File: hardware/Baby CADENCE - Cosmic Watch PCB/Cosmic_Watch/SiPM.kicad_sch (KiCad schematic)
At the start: 1 part, among them IC1 MICROFJ-60035-TSV-TR1

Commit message: Comments/Reminders
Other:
- note added: "Implement Bias Decoupling"
- note added: "Implement Bias Filter (here or in the signal processing schematic)"
- note added: "Implement Impedence Matching"
- moved on the sheet: IC1

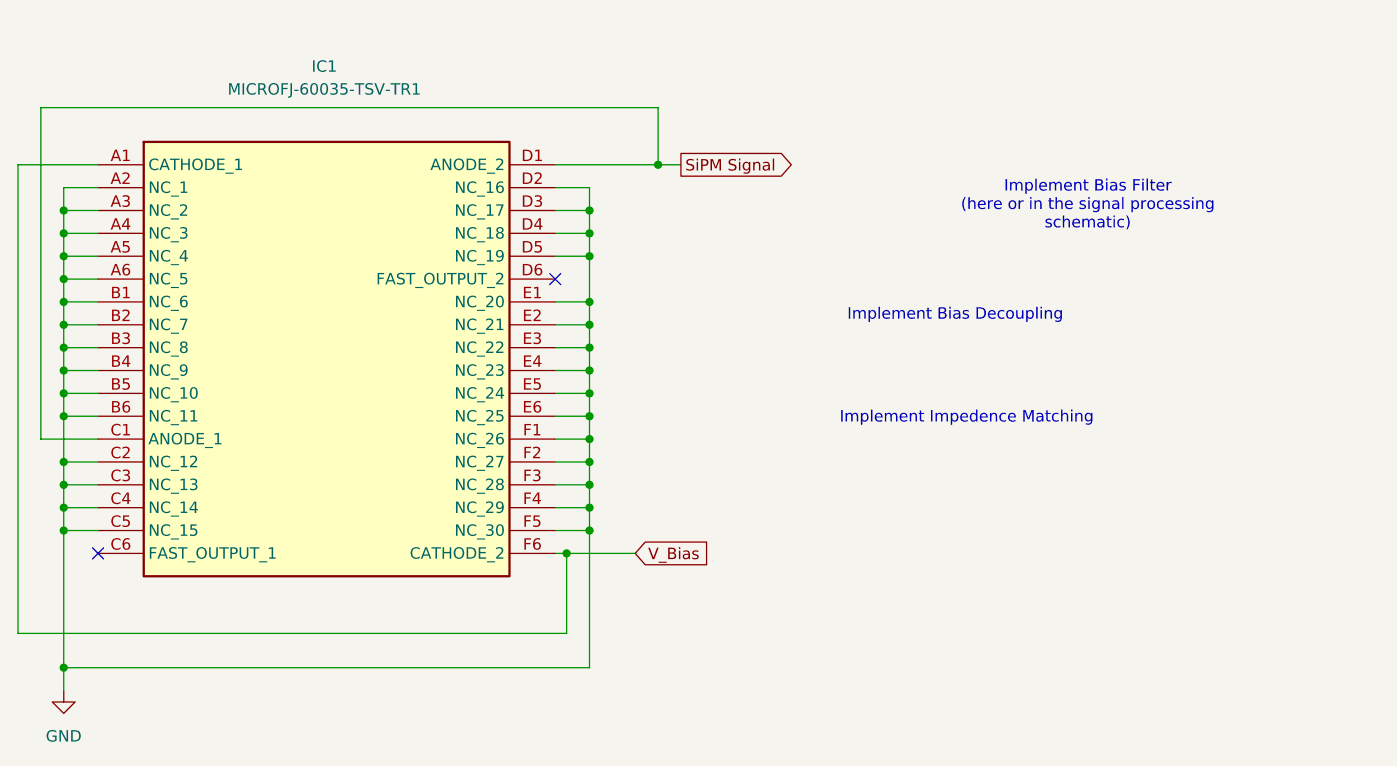
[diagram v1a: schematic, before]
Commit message: More Updates
Almost done with power.sch, just need to figure out ferrite bead values/other manufacturers since the old one is obsolete. Still figuring out values for the amplification stage.
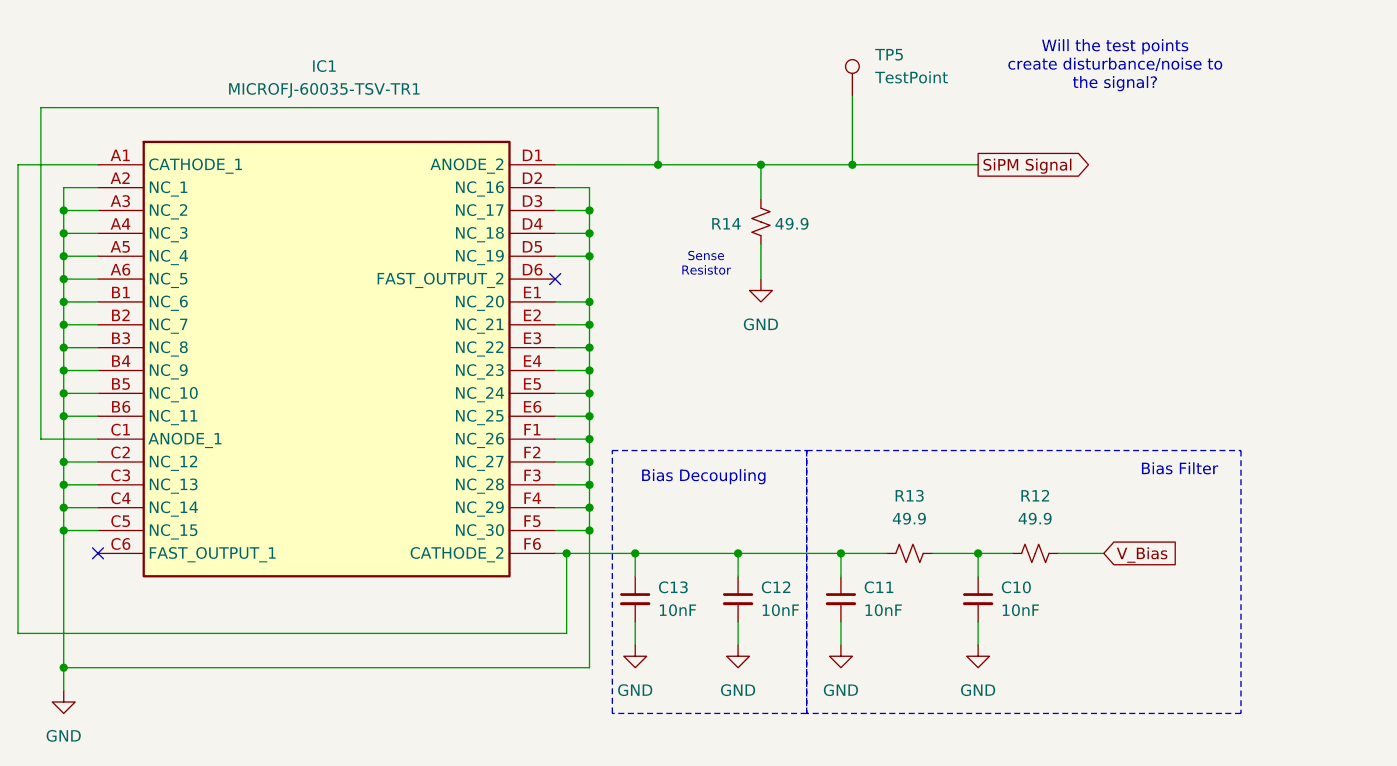
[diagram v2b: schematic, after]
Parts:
- added C10, C11, C12, C13: 10nF, symbol Device:C_Small
- added R12, R13, R14: 49.9, symbol Device:R_Small_US
- added TP5: TestPoint, symbol Connector:TestPoint
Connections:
- net GND: now also C10.2, C11.2, C12.2, C13.2, R14.2
- net SiPM Signal: now also R14.1, TP5.1
- net V_Bias: now also R12.2; no longer IC1.A1 (CATHODE_1), IC1.F6 (CATHODE_2)
- new net: C11.1, C12.1, C13.1, IC1.A1 (CATHODE_1), IC1.F6 (CATHODE_2), R13.1
- new net: C10.1, R12.1, R13.2
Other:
- note added: "Bias Decoupling"
- note added: "Bias Filter"
- note added: "Sense Resistor"
- note added: "Will the test points create disturbance/noise to the signal?"
- note removed: "Implement Bias Decoupling"
- note removed: "Implement Bias Filter (here or in the signal processing schematic)"
- note removed: "Implement Impedence Matching"

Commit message: Updates
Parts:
- TP5: value TestPoint -> Raw Signal Test Point
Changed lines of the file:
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@@
 	(text "Will the test points \ncreate disturbance/noise to\nthe signal?\n"
 		(exclude_from_sim no)
-		(at 154.94 24.638 0)
+		(at 167.894 22.86 0)
 		(effects
 			(font
@@
 		(on_board yes)
 		(dnp no)
-		(fields_autoplaced yes)
 		(property "Reference" "TP5"
-			(at 128.27 23.3679 0)
+			(at 128.27 25.654 0)
 			(effects
 				(font
@@
 			)
 		)
-		(property "Value" "TestPoint"
-			(at 128.27 25.9079 0)
-			(effects
-				(font
+		(property "Value" "Raw Signal Test Point"
+			(at 128.27 28.448 0)
+			(effects
+				(font
